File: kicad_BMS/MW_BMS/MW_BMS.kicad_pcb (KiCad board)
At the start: 4 copper layers, 51.3 x 56.1 mm, 83 parts, among them J1 Conn_01x02_Pin, J3 Conn_01x05_Pin, J4 Conn_01x02_Pin, Q1 CSD17578Q5A, Q3 NPN_BSS306NH6327XTSA1, Q4 PNP_BSS308PE, Q5 NPN_BSS306NH6327XTSA1, Q6 PNP_BSS308PE, T1 Transformer_1P_1S, U1 L9963E-TR, U2 USBLC6-2SC6Y, U3 USBLC6-2SC6Y

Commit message: pad gnd
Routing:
- net GNDD: track 28.3 -> 45.9 mm, vias 2 -> 4
- net GNDA: track 30.6 -> 35.3 mm, vias 7 -> 17
- net Net-(J4-Pin_1): track 0.00 -> 2.89 mm
- net /S14: track 18.6 -> 20.2 mm
- net GND_ESD: track 78.8 -> 80.4 mm, vias 16 -> 17
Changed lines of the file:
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@@
 		(capping no)
 		(filling no)
+		(grid_origin 145.9 97.7)
 		(pcbplotparams
 			(layerselection 0x00000000_00000000_55555555_5755f5ff)
@@
 	)
 	(segment
-		(start 152.4 80.1)
-		(end 159.4 87.1)
-		(width 0.2)
-		(layer "In2.Cu")
-		(net "/B14_13")
-	)
-	(segment
-		(start 169.7 94.2)
-		(end 169.7 98.9)
+		(start 151 80.1)
+		(end 152.4 80.1)
 		(width 0.2)
 		(layer "In2.Cu")
@@
 	)
 	(segment
-		(start 152.4 80.1)
-		(end 151 80.1)
+		(start 162.6 87.1)
+		(end 169.7 94.2)
 		(width 0.2)
 		(layer "In2.Cu")
@@
 	)
 	(segment
-		(start 162.6 87.1)
-		(end 169.7 94.2)
+		(start 159.4 87.1)
+		(end 162.6 87.1)
 		(width 0.2)
 		(layer "In2.Cu")
@@
 	)
 	(segment
+		(start 169.7 94.2)
+		(end 169.7 98.9)
+		(width 0.2)
+		(layer "In2.Cu")
+		(net "/B14_13")
+	)
+	(segment
 		(start 149.9 80.1)
 		(end 146.75 83.25)
@@
 	)
 	(segment
-		(start 159.4 87.1)
-		(end 162.6 87.1)
+		(start 152.4 80.1)
+		(end 159.4 87.1)
 		(width 0.2)
 		(layer "In2.Cu")
@@
 	)
 	(segment
+		(start 146.372785 107.572785)
+		(end 146.34557 107.6)
+		(width 0.2)
+		(layer "F.Cu")
+		(net "GNDA")
+	)
+	(segment
 		(start 140.99874 95.59874)
 		(end 140.6 95.2)
@@
 	)
 	(segment
+		(start 146.34557 107.6)
+		(end 146.3 107.6)
+		(width 0.2)
+		(layer "F.Cu")
+		(net "GNDA")
+	)
+	(segment
 		(start 141.9462 96.098866)
 		(end 141.9462 95.59874)
@@
 		(net "GNDA")
 	)
+	(segment
+		(start 146.372785 105.026585)
+		(end 146.372785 107.572785)
+		(width 0.2)
+		(layer "F.Cu")
+		(net "GNDA")
+	)
+	(via
+		(at 147.6231 99.349685)
+		(size 0.6)
+		(drill 0.3)
+		(layers "F.Cu" "B.Cu")
+		(net "GNDA")
+	)
+	(via
+		(at 146.4231 100.549685)
+		(size 0.6)
+		(drill 0.3)
+		(layers "F.Cu" "B.Cu")
+		(net "GNDA")
+	)
 	(via
 		(at 144.25 100.25)
@@
 	)
 	(via
+		(at 146.3 107.6)
+		(size 0.5)
+		(drill 0.3)
+		(layers "F.Cu" "B.Cu")
+		(net "GNDA")
+	)
+	(via
 		(at 130.2 103.8)
 		(size 0.6)
@@
 	)
 	(via
+		(at 147.6231 98.149685)
+		(size 0.6)
+		(drill 0.3)
+		(layers "F.Cu" "B.Cu")
+		(net "GNDA")
+	)
+	(via
 		(at 143 107.6)
 		(size 0.5)
@@
 	)
 	(via
+		(at 146.4231 99.349685)
+		(size 0.6)
+		(drill 0.3)
+		(layers "F.Cu" "B.Cu")
+		(net "GNDA")
+	)
+	(via
+		(at 147.6231 100.549685)
+		(size 0.6)
+		(drill 0.3)
+		(layers "F.Cu" "B.Cu")
+		(net "GNDA")
+	)
+	(via
+		(at 146.4231 98.149685)
+		(size 0.6)
+		(drill 0.3)
+		(layers "F.Cu" "B.Cu")
+		(net "GNDA")
+	)
+	(via
+		(at 148.8231 100.549685)
+		(size 0.6)
+		(drill 0.3)
+		(layers "F.Cu" "B.Cu")
+		(net "GNDA")
+	)
+	(via
 		(at 136.3 95.1)
 		(size 0.6)
@@
 	)
 	(via
+		(at 148.8231 98.149685)
+		(size 0.6)
+		(drill 0.3)
+		(layers "F.Cu" "B.Cu")
+		(net "GNDA")
+	)
+	(via
 		(at 135.2 109.6)
 		(size 0.6)
@@
 		(net "GNDA")
 	)
+	(via
+		(at 148.8231 99.349685)
+		(size 0.6)
+		(drill 0.3)
+		(layers "F.Cu" "B.Cu")
+		(net "GNDA")
+	)
 	(segment
 		(start 129.4 99.425)
@@
 	)
 	(segment
+		(start 146.3 107.6)
+		(end 144.2 107.6)
+		(width 0.2)
+		(layer "B.Cu")
+		(net "GNDA")
+	)
+	(segment
 		(start 144.2 100.3)
 		(end 144.25 100.25)
@@
 	)
 	(segment
+		(start 142.900252 99.599748)
+		(end 141.9462 99.599748)
+		(width 0.2)
+		(layer "F.Cu")
+		(net "GNDD")
+	)
+	(segment
+		(start 143.4 99.1)
+		(end 142.900252 99.599748)
+		(width 0.2)
+		(layer "F.Cu")
+		(net "GNDD")
+	)
+	(segment
+		(start 145.372533 105.026585)
+		(end 145.372533 106.572533)
+		(width 0.2)
+		(layer "F.Cu")
+		(net "GNDD")
+	)
+	(segment
+		(start 142.99937 98.09937)
+		(end 143.4 98.5)
+		(width 0.2)
+		(layer "F.Cu")
+		(net "GNDD")
+	)
+	(segment
 		(start 133.8 99.5)
 		(end 133.8 98.4)
@@
 	)
 	(segment
+		(start 140.399874 98.09937)
+		(end 140.3 98.199244)
+		(width 0.2)
+		(layer "F.Cu")
+		(net "GNDD")
+	)
+	(segment
+		(start 143.4 98.5)
+		(end 143.4 99.1)
+		(width 0.2)
+		(layer "F.Cu")
+		(net "GNDD")
+	)
+	(segment
+		(start 141.9462 98.09937)
+		(end 140.399874 98.09937)
+		(width 0.2)
+		(layer "F.Cu")
+		(net "GNDD")
+	)
+	(segment
 		(start 127.7 101.1)
 		(end 129.2 101.1)
@@
 		(net "GNDD")
 	)
+	(segment
+		(start 145.372533 106.572533)
+		(end 145.4 106.6)
+		(width 0.2)
+		(layer "F.Cu")
+		(net "GNDD")
+	)
+	(segment
+		(start 141.9462 98.09937)
+		(end 142.99937 98.09937)
+		(width 0.2)
+		(layer "F.Cu")
+		(net "GNDD")
+	)
 	(via
 		(at 129.2 101.1)
@@
 		(net "GNDD")
 	)
+	(via
+		(at 145.4 106.6)
+		(size 0.6)
+		(drill 0.3)
+		(layers "F.Cu" "B.Cu")
+		(net "GNDD")
+	)
+	(via
+		(at 140.3 98.199244)
+		(size 0.6)
+		(drill 0.3)
+		(layers "F.Cu" "B.Cu")
+		(net "GNDD")
+	)
 	(segment
 		(start 137.6 86.2)
@@
 	)
 	(segment
+		(start 145.4 106.6)
+		(end 140.3 101.5)
+		(width 0.2)
+		(layer "In2.Cu")
+		(net "GNDD")
+	)
+	(segment
+		(start 140.3 101.5)
+		(end 140.3 98.199244)
+		(width 0.2)
+		(layer "In2.Cu")
+		(net "GNDD")
+	)
+	(segment
 		(start 141.9462 99.099622)
 		(end 141.9462 98.599496)
@@
 	)
 	(segment
+		(start 164.1 120.9)
+		(end 164.1 122.5)
+		(width 0.2)
+		(layer "F.Cu")
+		(net "GND_ESD")
+	)
+	(segment
 		(start 165.4 93.9)
 		(end 165.5 94)
@@
 	)
 	(via
+		(at 164.1 122.5)
+		(size 0.6)
+		(drill 0.3)
+		(layers "F.Cu" "B.Cu")
+		(net "GND_ESD")
+	)
+	(via
 		(at 165.5 101.5)
 		(size 0.6)
@@
 	)
 	(segment
+		(start 145.85 92.55)
+		(end 146.2 92.2)
+		(width 0.2)
+		(layer "B.Cu")
+		(net "/S14")
+	)
+	(segment
+		(start 145.85 93.7)
+		(end 145.85 92.55)
+		(width 0.2)
+		(layer "B.Cu")
+		(net "/S14")
+	)
+	(segment
 		(start 143.2 87.5)
 		(end 146.2 90.5)
@@
 	)
 	(segment
+		(start 130.519498 102.35)
+		(end 130.5695 102.400002)
+		(width 0.2)
+		(layer "F.Cu")
+		(net "Net-(J4-Pin_1)")
+	)
+	(segment
+		(start 127.7 102.35)
+		(end 130.519498 102.35)
+		(width 0.2)
+		(layer "F.Cu")
+		(net "Net-(J4-Pin_1)")
+	)
+	(segment

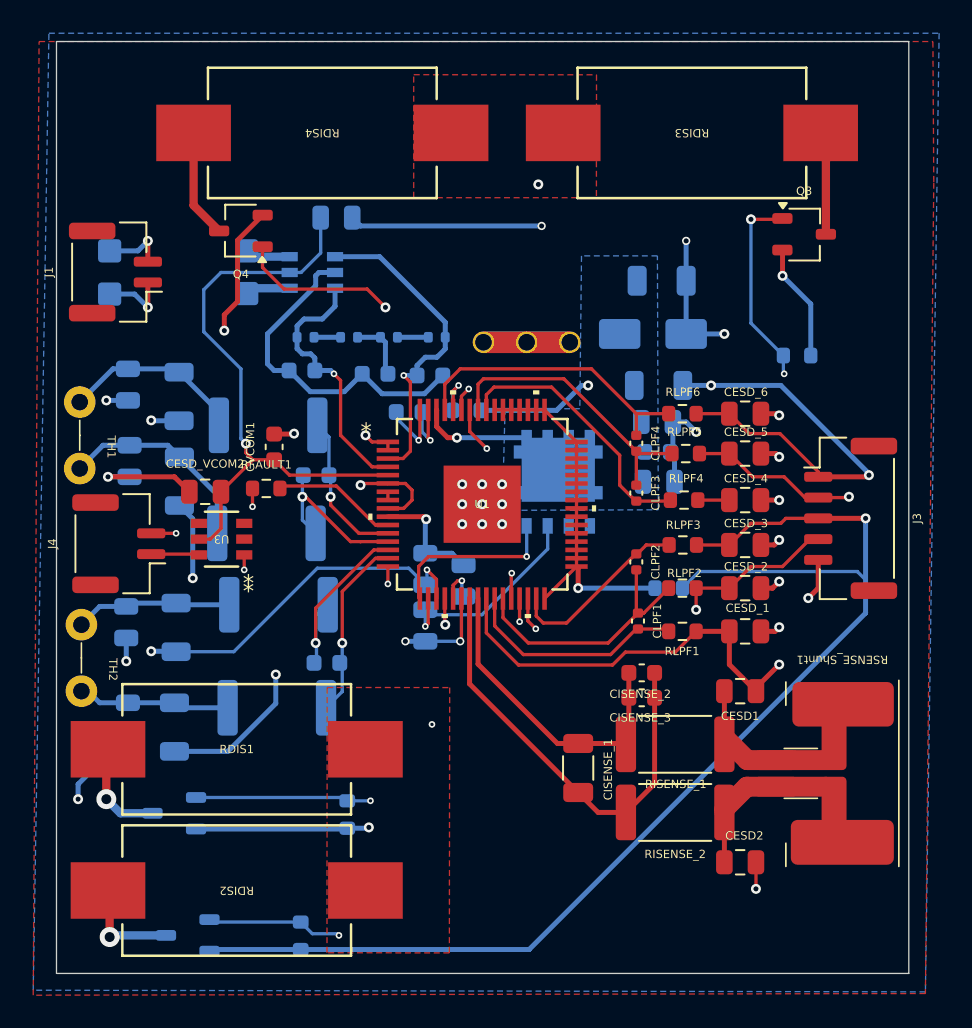
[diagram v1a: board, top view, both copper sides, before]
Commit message: fixing DRC errors
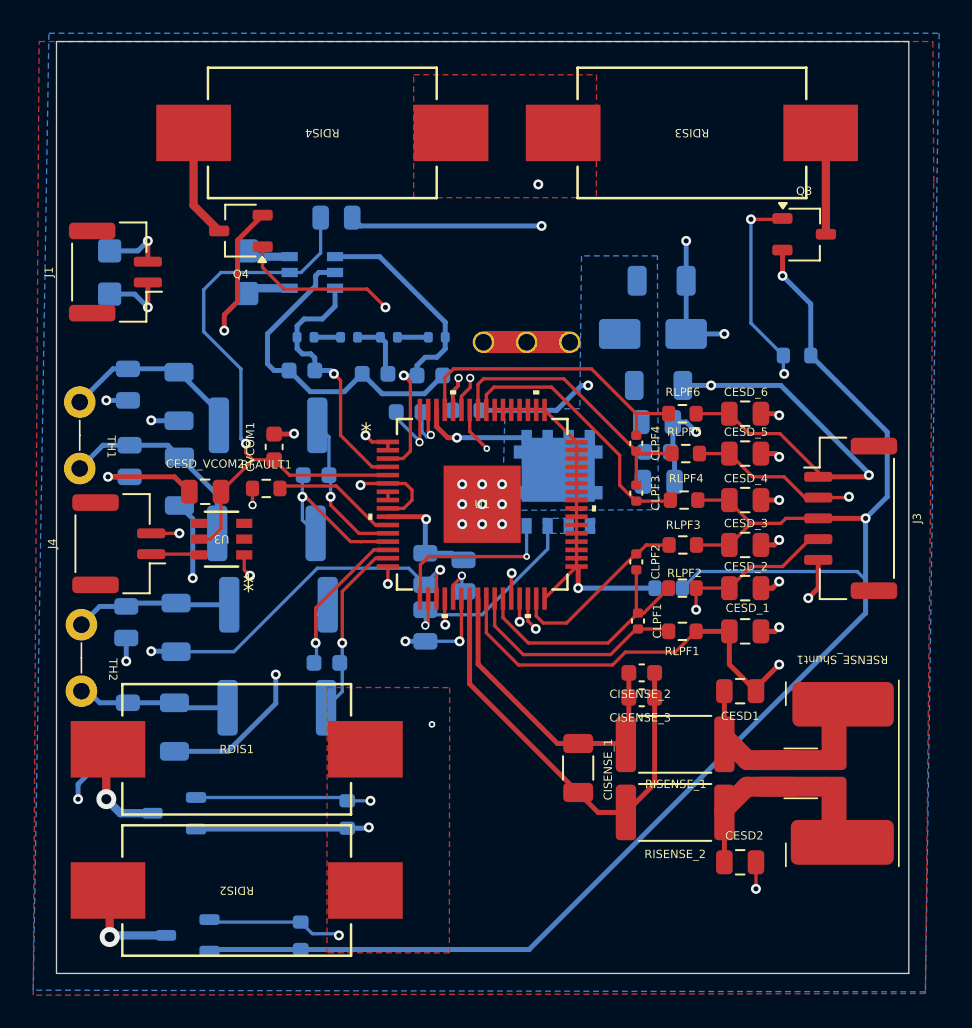
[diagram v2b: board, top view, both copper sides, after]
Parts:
- moved CVANA1 0.30 mm to (146.5, 103.7)
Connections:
- CESD_4 pad 1: /CELL3_minus -> /CELL2_plus
- Q3 pad 2: /CELL3_minus -> /CELL2_plus
- RDRV3 pad 1: /CELL3_minus -> /CELL2_plus
- RLPF4 pad 1: /CELL3_minus -> /CELL2_plus
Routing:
- net /CELL2_plus: track 76.5 -> 99.6 mm, vias 1 -> 2
- net /CELL3_minus: track 8.96 -> 0.00 mm, vias 1 -> 0
- added copper zone on B.Cu, net /VREG
